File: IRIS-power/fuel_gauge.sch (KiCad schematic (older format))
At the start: 10 parts

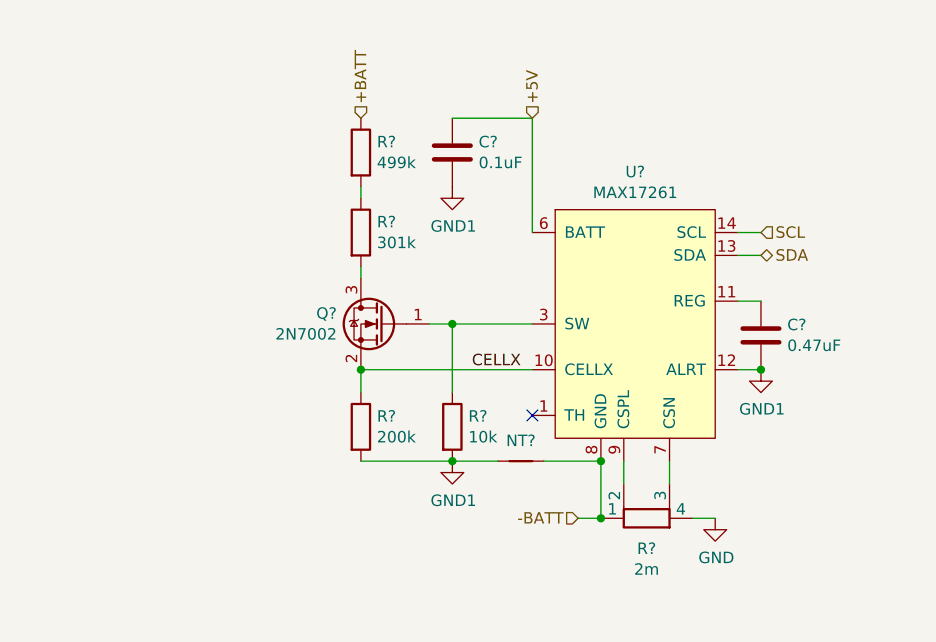
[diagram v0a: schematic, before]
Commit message: Finalized power board V2 schematic, preparing to layout
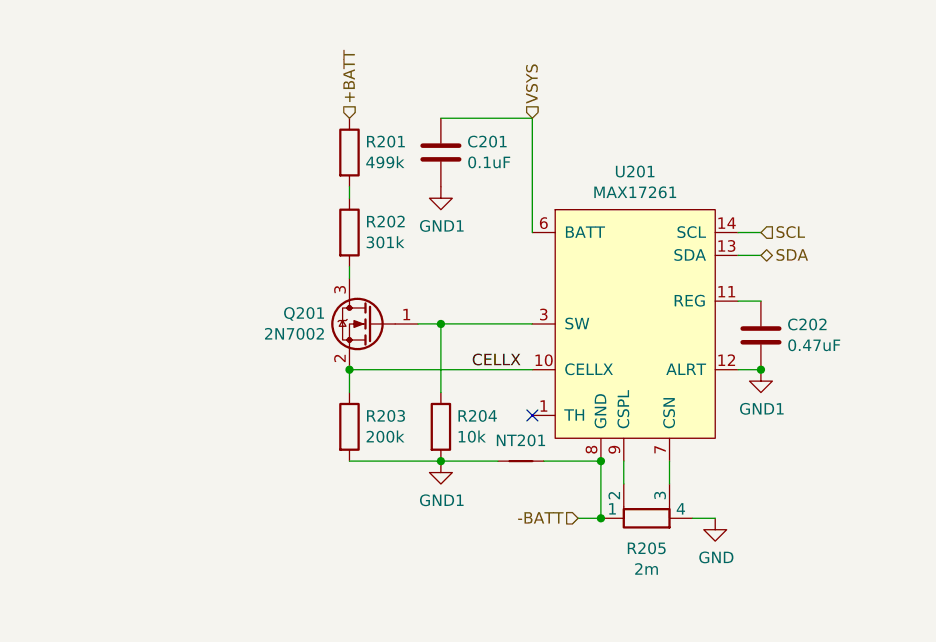
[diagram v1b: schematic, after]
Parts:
- C201, C202: renamed from C?; footprint (none) -> Capacitor_SMD:C_0603_1608Metric
- NT201: renamed from NT?; footprint (none) -> NetTie:NetTie-2_SMD_Pad0.5mm
- R201, R202, R203, R204: renamed from R?; footprint (none) -> Resistor_SMD:R_0603_1608Metric
- R205: renamed from R?; footprint (none) -> star-common-lib:CST0612-FC-R002E; Digikey PN (none) -> CST0612-FC-R002ECT-ND; MFG PN (none) -> CST0612-FC-R002E; Unit Cost (none) -> 0.78
- U201: renamed from U?; footprint (none) -> Package_DFN_QFN:DFN-14-1EP_3x3mm_P0.4mm_EP1.78x2.35mm
- gave numbers to parts that had none: 1
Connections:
- net +5V renamed VSYS
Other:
- moved on the sheet: C201, Q201, R201, R202, R203, R204
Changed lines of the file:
@@
 $Descr A4 11693 8268
 encoding utf-8
-Sheet 7 9
+Sheet 2 8
 Title ""
 Date ""
@@
 Wire Wire Line
 	5800 3100 5800 3600
-Wire Wire Line
-	5450 3100 5800 3100
 Text Label 5750 4200 2    50   ~ 0
 CELLX
 Wire Wire Line
-	5050 3450 5050 3400
-Wire Wire Line
-	5050 3750 5050 3800
+	5000 3450 5000 3400
+Wire Wire Line
+	5000 3750 5000 3800
 $Comp
 L power:GND1 #PWR?
 U 1 1 5F3ED548
-P 5450 4600
+P 5400 4600
 AR Path="/5F3ED548" Ref="#PWR?"  Part="1"
-AR Path="/5F3CDA08/5F3ED548" Ref="#PWR?"  Part="1"
-F 0 "#PWR?" H 5450 4350 50  0001 C CNN
-F 1 "GND1" H 5455 4427 50  0000 C CNN
-F 2 "" H 5450 4600 50  0001 C CNN
-F 3 "" H 5450 4600 50  0001 C CNN
-	1    5450 4600
+AR Path="/5F3CDA08/5F3ED548" Ref="#PWR0202"  Part="1"
+F 0 "#PWR0202" H 5400 4350 50  0001 C CNN
+F 1 "GND1" H 5405 4427 50  0000 C CNN
+F 2 "" H 5400 4600 50  0001 C CNN
+F 3 "" H 5400 4600 50  0001 C CNN
+	1    5400 4600
 	1    0    0    -1
 $EndComp
@@
 P 6800 4200
 AR Path="/5F3ED54F" Ref="#PWR?"  Part="1"
-AR Path="/5F3CDA08/5F3ED54F" Ref="#PWR?"  Part="1"
-F 0 "#PWR?" H 6800 3950 50  0001 C CNN
+AR Path="/5F3CDA08/5F3ED54F" Ref="#PWR0204"  Part="1"
+F 0 "#PWR0204" H 6800 3950 50  0001 C CNN
 F 1 "GND1" H 6805 4027 50  0000 C CNN
 F 2 "" H 6800 4200 50  0001 C CNN
@@
 L power:GND1 #PWR?
 U 1 1 5F3ED555
-P 5450 3400
+P 5400 3400
 AR Path="/5F3ED555" Ref="#PWR?"  Part="1"
-AR Path="/5F3CDA08/5F3ED555" Ref="#PWR?"  Part="1"
-F 0 "#PWR?" H 5450 3150 50  0001 C CNN
-F 1 "GND1" H 5455 3227 50  0000 C CNN
-F 2 "" H 5450 3400 50  0001 C CNN
-F 3 "" H 5450 3400 50  0001 C CNN
-	1    5450 3400
+AR Path="/5F3CDA08/5F3ED555" Ref="#PWR0201"  Part="1"
+F 0 "#PWR0201" H 5400 3150 50  0001 C CNN
+F 1 "GND1" H 5405 3227 50  0000 C CNN
+F 2 "" H 5400 3400 50  0001 C CNN
+F 3 "" H 5400 3400 50  0001 C CNN
+	1    5400 3400
 	1    0    0    -1
 $EndComp
@@
 P 5750 4600
 AR Path="/5F3ED55B" Ref="NT?"  Part="1"
-AR Path="/5F3CDA08/5F3ED55B" Ref="NT?"  Part="1"
-F 0 "NT?" H 5750 4689 50  0000 C CNN
+AR Path="/5F3CDA08/5F3ED55B" Ref="NT201"  Part="1"
+F 0 "NT201" H 5750 4689 50  0000 C CNN
 F 1 "Net-Tie_2" H 5750 4690 50  0001 C CNN
-F 2 "" H 5750 4600 50  0001 C CNN
+F 2 "NetTie:NetTie-2_SMD_Pad0.5mm" H 5750 4600 50  0001 C CNN
 F 3 "~" H 5750 4600 50  0001 C CNN
 	1    5750 4600
@@
 P 6600 4850
 AR Path="/5F3ED567" Ref="#PWR?"  Part="1"
-AR Path="/5F3CDA08/5F3ED567" Ref="#PWR?"  Part="1"
-F 0 "#PWR?" H 6600 4600 50  0001 C CNN
+AR Path="/5F3CDA08/5F3ED567" Ref="#PWR0203"  Part="1"
+F 0 "#PWR0203" H 6600 4600 50  0001 C CNN
 F 1 "GND" H 6605 4677 50  0000 C CNN
 F 2 "" H 6600 4850 50  0001 C CNN
@@
 L Device:R R?
 U 1 1 5F3ED56F
-P 5450 4450
+P 5400 4450
 AR Path="/5F3ED56F" Ref="R?"  Part="1"
-AR Path="/5F3CDA08/5F3ED56F" Ref="R?"  Part="1"
-F 0 "R?" H 5520 4496 50  0000 L CNN
-F 1 "10k" H 5520 4405 50  0000 L CNN
-F 2 "" V 5380 4450 50  0001 C CNN
-F 3 "~" H 5450 4450 50  0001 C CNN
-	1    5450 4450
+AR Path="/5F3CDA08/5F3ED56F" Ref="R204"  Part="1"
+F 0 "R204" H 5470 4496 50  0000 L CNN
+F 1 "10k" H 5470 4405 50  0000 L CNN
+F 2 "Resistor_SMD:R_0603_1608Metric" V 5330 4450 50  0001 C CNN
+F 3 "~" H 5400 4450 50  0001 C CNN
+	1    5400 4450
 	1    0    0    -1
 $EndComp
@@
 L Device:C C?
 U 1 1 5F3ED575
-P 5450 3250
+P 5400 3250
 AR Path="/5F3ED575" Ref="C?"  Part="1"
-AR Path="/5F3CDA08/5F3ED575" Ref="C?"  Part="1"
-F 0 "C?" H 5565 3296 50  0000 L CNN
-F 1 "0.1uF" H 5565 3205 50  0000 L CNN
-F 2 "" H 5488 3100 50  0001 C CNN
-F 3 "~" H 5450 3250 50  0001 C CNN
-	1    5450 3250
+AR Path="/5F3CDA08/5F3ED575" Ref="C201"  Part="1"
+F 0 "C201" H 5515 3296 50  0000 L CNN
+F 1 "0.1uF" H 5515 3205 50  0000 L CNN
+F 2 "Capacitor_SMD:C_0603_1608Metric" H 5438 3100 50  0001 C CNN
+F 3 "~" H 5400 3250 50  0001 C CNN
+	1    5400 3250
 	1    0    0    -1
 $EndComp
@@
 P 6800 4050
 AR Path="/5F3ED581" Ref="C?"  Part="1"
-AR Path="/5F3CDA08/5F3ED581" Ref="C?"  Part="1"
-F 0 "C?" H 6915 4096 50  0000 L CNN
+AR Path="/5F3CDA08/5F3ED581" Ref="C202"  Part="1"
+F 0 "C202" H 6915 4096 50  0000 L CNN
 F 1 "0.47uF" H 6915 4005 50  0000 L CNN
-F 2 "" H 6838 3900 50  0001 C CNN
+F 2 "Capacitor_SMD:C_0603_1608Metric" H 6838 3900 50  0001 C CNN
 F 3 "~" H 6800 4050 50  0001 C CNN
 	1    6800 4050
@@
 $EndComp
 Wire Wire Line
-	5050 4300 5050 4200
+	5000 4300 5000 4200
 $Comp
 L Device:R R?
 U 1 1 5F3ED58E
-P 5050 3250
+P 5000 3250
 AR Path="/5F3ED58E" Ref="R?"  Part="1"
-AR Path="/5F3CDA08/5F3ED58E" Ref="R?"  Part="1"
-F 0 "R?" H 5120 3296 50  0000 L CNN
-F 1 "499k" H 5120 3205 50  0000 L CNN
-F 2 "" V 4980 3250 50  0001 C CNN
-F 3 "~" H 5050 3250 50  0001 C CNN
-	1    5050 3250
+AR Path="/5F3CDA08/5F3ED58E" Ref="R201"  Part="1"
+F 0 "R201" H 5070 3296 50  0000 L CNN
+F 1 "499k" H 5070 3205 50  0000 L CNN
+F 2 "Resistor_SMD:R_0603_1608Metric" V 4930 3250 50  0001 C CNN
+F 3 "~" H 5000 3250 50  0001 C CNN
+	1    5000 3250
 	1    0    0    -1
 $EndComp
@@
 L Device:R R?
 U 1 1 5F3ED594
-P 5050 3600
+P 5000 3600
 AR Path="/5F3ED594" Ref="R?"  Part="1"
-AR Path="/5F3CDA08/5F3ED594" Ref="R?"  Part="1"
-F 0 "R?" H 5120 3646 50  0000 L CNN
-F 1 "301k" H 5120 3555 50  0000 L CNN
-F 2 "" V 4980 3600 50  0001 C CNN
-F 3 "~" H 5050 3600 50  0001 C CNN
-	1    5050 3600
+AR Path="/5F3CDA08/5F3ED594" Ref="R202"  Part="1"
+F 0 "R202" H 5070 3646 50  0000 L CNN
+F 1 "301k" H 5070 3555 50  0000 L CNN
+F 2 "Resistor_SMD:R_0603_1608Metric" V 4930 3600 50  0001 C CNN
+F 3 "~" H 5000 3600 50  0001 C CNN
+	1    5000 3600
 	1    0    0    -1
 $EndComp
@@
 L Device:R R?
 U 1 1 5F3ED59A
-P 5050 4450
+P 5000 4450
 AR Path="/5F3ED59A" Ref="R?"  Part="1"
-AR Path="/5F3CDA08/5F3ED59A" Ref="R?"  Part="1"
-F 0 "R?" H 5120 4496 50  0000 L CNN
-F 1 "200k" H 5120 4405 50  0000 L CNN
-F 2 "" V 4980 4450 50  0001 C CNN
-F 3 "~" H 5050 4450 50  0001 C CNN
-	1    5050 4450
+AR Path="/5F3CDA08/5F3ED59A" Ref="R203"  Part="1"
+F 0 "R203" H 5070 4496 50  0000 L CNN
+F 1 "200k" H 5070 4405 50  0000 L CNN
+F 2 "Resistor_SMD:R_0603_1608Metric" V 4930 4450 50  0001 C CNN
+F 3 "~" H 5000 4450 50  0001 C CNN
+	1    5000 4450
 	1    0    0    -1
 $EndComp
@@
 L Transistor_FET:2N7002 Q?
 U 1 1 5F3ED5A0
-P 5150 4000
+P 5100 4000
 AR Path="/5F3ED5A0" Ref="Q?"  Part="1"
-AR Path="/5F3CDA08/5F3ED5A0" Ref="Q?"  Part="1"
-F 0 "Q?" H 5355 4046 50  0000 L CNN
-F 1 "2N7002" H 5355 3955 50  0000 L CNN
-F 2 "Package_TO_SOT_SMD:SOT-23" H 5350 3925 50  0001 L CIN
-F 3 "https://www.fairchildsemi.com/datasheets/2N/2N7002.pdf" H 5150 4000 50  0001 L CNN
-	1    5150 4000
+AR Path="/5F3CDA08/5F3ED5A0" Ref="Q201"  Part="1"
+F 0 "Q201" H 5305 4046 50  0000 L CNN
+F 1 "2N7002" H 5305 3955 50  0000 L CNN
+F 2 "Package_TO_SOT_SMD:SOT-23" H 5300 3925 50  0001 L CIN
+F 3 "https://www.fairchildsemi.com/datasheets/2N/2N7002.pdf" H 5100 4000 50  0001 L CNN
+	1    5100 4000
 	-1   0    0    -1
 $EndComp
@@
 P 6300 4850
 AR Path="/5F3ED5AE" Ref="R?"  Part="1"
-AR Path="/5F3CDA08/5F3ED5AE" Ref="R?"  Part="1"
-F 0 "R?" V 6167 4850 50  0000 C CNN
+AR Path="/5F3CDA08/5F3ED5AE" Ref="R205"  Part="1"
+F 0 "R205" V 6167 4850 50  0000 C CNN
 F 1 "2m" V 6076 4850 50  0000 C CNN
-F 2 "" V 6230 4850 50  0001 C CNN
-F 3 "~" H 6300 4850 50  0001 C CNN
+F 2 "star-common-lib:CST0612-FC-R002E" V 6230 4850 50  0001 C CNN
+F 3 "https://www.bourns.com/docs/product-datasheets/cst0612.pdf" H 6300 4850 50  0001 C CNN
+F 4 "CST0612-FC-R002ECT-ND" H 6300 4850 50  0001 C CNN "Digikey PN"
+F 5 "CST0612-FC-R002E" H 6300 4850 50  0001 C CNN "MFG PN"
+F 6 "0.78" H 6300 4850 50  0001 C CNN "Unit Cost"
 	1    6300 4850
 	0    -1   -1   0
@@
 P 6250 4000
 AR Path="/5F3ED5B4" Ref="U?"  Part="1"
-AR Path="/5F3CDA08/5F3ED5B4" Ref="U?"  Part="1"
-F 0 "U?" H 6250 4665 50  0000 C CNN
+AR Path="/5F3CDA08/5F3ED5B4" Ref="U201"  Part="1"
+F 0 "U201" H 6250 4665 50  0000 C CNN
 F 1 "MAX17261" H 6250 4574 50  0000 C CNN
-F 2 "" H 6250 4000 50  0001 C CNN
+F 2 "Package_DFN_QFN:DFN-14-1EP_3x3mm_P0.4mm_EP1.78x2.35mm" H 6250 4000 50  0001 C CNN
 F 3 "" H 6250 4000 50  0001 C CNN
 	1    6250 4000
@@
 $EndComp
 Wire Wire Line
-	5450 4300 5450 4000
-Wire Wire Line
-	5800 4200 5050 4200
-Connection ~ 5050 4200
-Connection ~ 5450 4000
-Wire Wire Line
-	5450 4000 5800 4000
-Connection ~ 5450 4600
-Wire Wire Line
-	5450 4600 5650 4600
-Wire Wire Line
-	5350 4000 5450 4000
-Wire Wire Line
-	5050 4600 5450 4600
-Text HLabel 5050 3100 1    50   Input ~ 0
+	5400 4300 5400 4000
+Connection ~ 5000 4200
+Connection ~ 5400 4000
+Connection ~ 5400 4600
+Wire Wire Line
+	5300 4000 5400 4000
+Wire Wire Line
+	5000 4600 5400 4600
+Text HLabel 5000 3100 1    50   Input ~ 0
 +BATT
-Text HLabel 5800 3100 1    50   Input ~ 0
-+5V
 Text HLabel 6000 4850 0    50   Input ~ 0
 -BATT
@@
 Wire Wire Line
 	6700 3700 6800 3700
+Text HLabel 5800 3100 1    50   Input ~ 0
+VSYS
+Wire Wire Line
+	5400 4600 5650 4600
+Wire Wire Line
+	5000 4200 5800 4200
+Wire Wire Line
+	5400 4000 5800 4000
+Wire Wire Line
+	5400 3100 5800 3100
 $EndSCHEMATC

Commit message: Updated layout
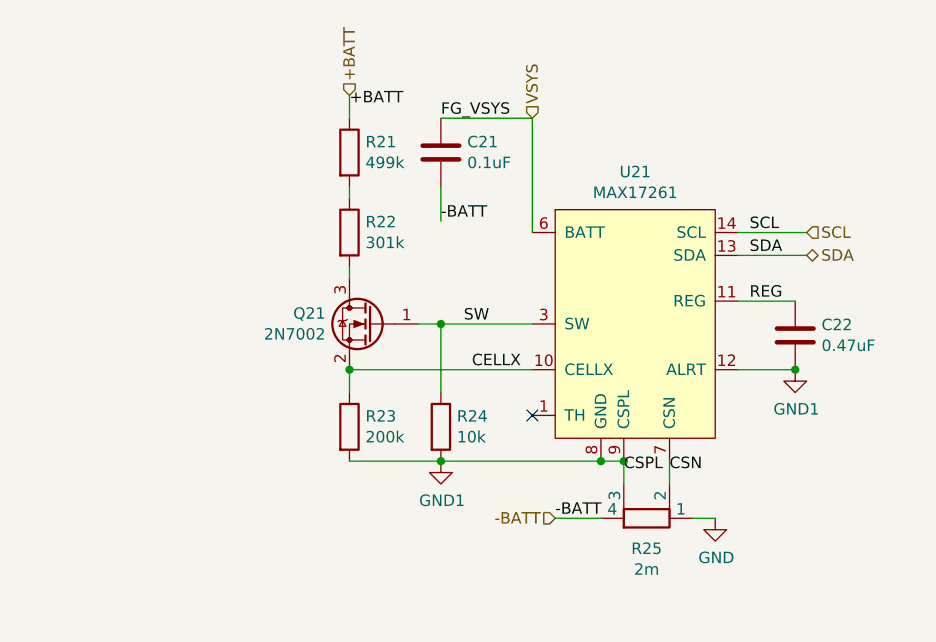
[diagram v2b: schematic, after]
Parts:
- removed NT201: Net-Tie_2, NetTie:NetTie-2_SMD_Pad0.5mm, symbol Device:Net-Tie_2
- U21: renamed from U201; footprint Package_DFN_QFN:DFN-14-1EP_3x3mm_P0.4mm_EP1.78x2.35mm -> star-common-lib:MAX17261
- renumbered C201 to C21, C202 to C22, Q201 to Q21, R201 to R21, R202 to R22, R203 to R23, R204 to R24, R205 to R25
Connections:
- net -BATT: now also C21.2, R25.4; no longer R25.1, U21.15, U21.8 (GND)
- net GND: now also R25.1; no longer R25.4
- net GND1: now also R25.3, U21.15, U21.8 (GND), U21.9 (CSPL); no longer C21.2
- net SW: now reaches Q21.1 (G), R24.1, U21.3 (SW)
- net REG: now reaches C22.1, U21.11 (REG)
- net CSN: now reaches R25.2
- net CSN: now also U21.7 (CSN); no longer U21.9 (CSPL)
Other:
- moved on the sheet: C22
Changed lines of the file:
@@
 P 5400 4600
 AR Path="/5F3ED548" Ref="#PWR?"  Part="1"
-AR Path="/5F3CDA08/5F3ED548" Ref="#PWR0202"  Part="1"
-F 0 "#PWR0202" H 5400 4350 50  0001 C CNN
+AR Path="/5F3CDA08/5F3ED548" Ref="#PWR021"  Part="1"
+F 0 "#PWR021" H 5400 4350 50  0001 C CNN
 F 1 "GND1" H 5405 4427 50  0000 C CNN
 F 2 "" H 5400 4600 50  0001 C CNN
@@
 	1    0    0    -1
 $EndComp
-Connection ~ 6800 4200
+Connection ~ 6950 4200
 $Comp
 L power:GND1 #PWR?
 U 1 1 5F3ED54F
-P 6800 4200
+P 6950 4200
 AR Path="/5F3ED54F" Ref="#PWR?"  Part="1"
-AR Path="/5F3CDA08/5F3ED54F" Ref="#PWR0204"  Part="1"
-F 0 "#PWR0204" H 6800 3950 50  0001 C CNN
-F 1 "GND1" H 6805 4027 50  0000 C CNN
-F 2 "" H 6800 4200 50  0001 C CNN
-F 3 "" H 6800 4200 50  0001 C CNN
-	1    6800 4200
-	1    0    0    -1
-$EndComp
-$Comp
-L power:GND1 #PWR?
-U 1 1 5F3ED555
-P 5400 3400
-AR Path="/5F3ED555" Ref="#PWR?"  Part="1"
-AR Path="/5F3CDA08/5F3ED555" Ref="#PWR0201"  Part="1"
-F 0 "#PWR0201" H 5400 3150 50  0001 C CNN
-F 1 "GND1" H 5405 3227 50  0000 C CNN
-F 2 "" H 5400 3400 50  0001 C CNN
-F 3 "" H 5400 3400 50  0001 C CNN
-	1    5400 3400
-	1    0    0    -1
-$EndComp
-$Comp
-L Device:Net-Tie_2 NT?
-U 1 1 5F3ED55B
-P 5750 4600
-AR Path="/5F3ED55B" Ref="NT?"  Part="1"
-AR Path="/5F3CDA08/5F3ED55B" Ref="NT201"  Part="1"
-F 0 "NT201" H 5750 4689 50  0000 C CNN
-F 1 "Net-Tie_2" H 5750 4690 50  0001 C CNN
-F 2 "NetTie:NetTie-2_SMD_Pad0.5mm" H 5750 4600 50  0001 C CNN
-F 3 "~" H 5750 4600 50  0001 C CNN
-	1    5750 4600
+AR Path="/5F3CDA08/5F3ED54F" Ref="#PWR023"  Part="1"
+F 0 "#PWR023" H 6950 3950 50  0001 C CNN
+F 1 "GND1" H 6955 4027 50  0000 C CNN
+F 2 "" H 6950 4200 50  0001 C CNN
+F 3 "" H 6950 4200 50  0001 C CNN
+	1    6950 4200
 	1    0    0    -1
 $EndComp
@@
 P 6600 4850
 AR Path="/5F3ED567" Ref="#PWR?"  Part="1"
-AR Path="/5F3CDA08/5F3ED567" Ref="#PWR0203"  Part="1"
-F 0 "#PWR0203" H 6600 4600 50  0001 C CNN
+AR Path="/5F3CDA08/5F3ED567" Ref="#PWR022"  Part="1"
+F 0 "#PWR022" H 6600 4600 50  0001 C CNN
 F 1 "GND" H 6605 4677 50  0000 C CNN
 F 2 "" H 6600 4850 50  0001 C CNN
@@
 	1    0    0    -1
 $EndComp
-Wire Wire Line
-	6700 4200 6800 4200
 NoConn ~ 5800 4400
 $Comp
@@
 P 5400 4450
 AR Path="/5F3ED56F" Ref="R?"  Part="1"
-AR Path="/5F3CDA08/5F3ED56F" Ref="R204"  Part="1"
-F 0 "R204" H 5470 4496 50  0000 L CNN
+AR Path="/5F3CDA08/5F3ED56F" Ref="R24"  Part="1"
+F 0 "R24" H 5470 4496 50  0000 L CNN
 F 1 "10k" H 5470 4405 50  0000 L CNN
 F 2 "Resistor_SMD:R_0603_1608Metric" V 5330 4450 50  0001 C CNN
@@
 P 5400 3250
 AR Path="/5F3ED575" Ref="C?"  Part="1"
-AR Path="/5F3CDA08/5F3ED575" Ref="C201"  Part="1"
-F 0 "C201" H 5515 3296 50  0000 L CNN
+AR Path="/5F3CDA08/5F3ED575" Ref="C21"  Part="1"
+F 0 "C21" H 5515 3296 50  0000 L CNN
 F 1 "0.1uF" H 5515 3205 50  0000 L CNN
 F 2 "Capacitor_SMD:C_0603_1608Metric" H 5438 3100 50  0001 C CNN
@@
 	1    0    0    -1
 $EndComp
-Wire Wire Line
-	6700 3900 6800 3900
 $Comp
 L Device:C C?
 U 1 1 5F3ED581
-P 6800 4050
+P 6950 4050
 AR Path="/5F3ED581" Ref="C?"  Part="1"
-AR Path="/5F3CDA08/5F3ED581" Ref="C202"  Part="1"
-F 0 "C202" H 6915 4096 50  0000 L CNN
-F 1 "0.47uF" H 6915 4005 50  0000 L CNN
-F 2 "Capacitor_SMD:C_0603_1608Metric" H 6838 3900 50  0001 C CNN
-F 3 "~" H 6800 4050 50  0001 C CNN
-	1    6800 4050
+AR Path="/5F3CDA08/5F3ED581" Ref="C22"  Part="1"
+F 0 "C22" H 7065 4096 50  0000 L CNN
+F 1 "0.47uF" H 7065 4005 50  0000 L CNN
+F 2 "Capacitor_SMD:C_0603_1608Metric" H 6988 3900 50  0001 C CNN
+F 3 "~" H 6950 4050 50  0001 C CNN
+	1    6950 4050
 	1    0    0    -1
 $EndComp
@@
 P 5000 3250
 AR Path="/5F3ED58E" Ref="R?"  Part="1"
-AR Path="/5F3CDA08/5F3ED58E" Ref="R201"  Part="1"
-F 0 "R201" H 5070 3296 50  0000 L CNN
+AR Path="/5F3CDA08/5F3ED58E" Ref="R21"  Part="1"
+F 0 "R21" H 5070 3296 50  0000 L CNN
 F 1 "499k" H 5070 3205 50  0000 L CNN
 F 2 "Resistor_SMD:R_0603_1608Metric" V 4930 3250 50  0001 C CNN
@@
 P 5000 3600
 AR Path="/5F3ED594" Ref="R?"  Part="1"
-AR Path="/5F3CDA08/5F3ED594" Ref="R202"  Part="1"
-F 0 "R202" H 5070 3646 50  0000 L CNN
+AR Path="/5F3CDA08/5F3ED594" Ref="R22"  Part="1"
+F 0 "R22" H 5070 3646 50  0000 L CNN
 F 1 "301k" H 5070 3555 50  0000 L CNN
 F 2 "Resistor_SMD:R_0603_1608Metric" V 4930 3600 50  0001 C CNN
@@
 P 5000 4450
 AR Path="/5F3ED59A" Ref="R?"  Part="1"
-AR Path="/5F3CDA08/5F3ED59A" Ref="R203"  Part="1"
-F 0 "R203" H 5070 4496 50  0000 L CNN
+AR Path="/5F3CDA08/5F3ED59A" Ref="R23"  Part="1"
+F 0 "R23" H 5070 4496 50  0000 L CNN
 F 1 "200k" H 5070 4405 50  0000 L CNN
 F 2 "Resistor_SMD:R_0603_1608Metric" V 4930 4450 50  0001 C CNN
@@
 P 5100 4000
 AR Path="/5F3ED5A0" Ref="Q?"  Part="1"
-AR Path="/5F3CDA08/5F3ED5A0" Ref="Q201"  Part="1"
-F 0 "Q201" H 5305 4046 50  0000 L CNN
+AR Path="/5F3CDA08/5F3ED5A0" Ref="Q21"  Part="1"
+F 0 "Q21" H 5305 4046 50  0000 L CNN
 F 1 "2N7002" H 5305 3955 50  0000 L CNN
 F 2 "Package_TO_SOT_SMD:SOT-23" H 5300 3925 50  0001 L CIN
@@
 P 6300 4850
 AR Path="/5F3ED5AE" Ref="R?"  Part="1"
-AR Path="/5F3CDA08/5F3ED5AE" Ref="R205"  Part="1"
-F 0 "R205" V 6167 4850 50  0000 C CNN
+AR Path="/5F3CDA08/5F3ED5AE" Ref="R25"  Part="1"
+F 0 "R25" V 6167 4850 50  0000 C CNN
 F 1 "2m" V 6076 4850 50  0000 C CNN
 F 2 "star-common-lib:CST0612-FC-R002E" V 6230 4850 50  0001 C CNN
@@
 F 6 "0.78" H 6300 4850 50  0001 C CNN "Unit Cost"
 	1    6300 4850
-	0    -1   -1   0
-$EndComp
+	0    1    -1   0
+$EndComp
+Wire Wire Line
+	5400 4300 5400 4000
+Connection ~ 5000 4200
+Connection ~ 5400 4000
+Connection ~ 5400 4600
+Wire Wire Line
+	5300 4000 5400 4000
+Wire Wire Line
+	5000 4600 5400 4600
+Text HLabel 5000 3000 1    50   Input ~ 0
++BATT
+Text HLabel 5900 4850 0    50   Input ~ 0
+-BATT
+Wire Wire Line
+	6600 4850 6500 4850
+Text HLabel 7000 3600 2    50   Input ~ 0
+SCL
+Text HLabel 7000 3700 2    50   BiDi ~ 0
+SDA
+Text HLabel 5800 3100 1    50   Input ~ 0
+VSYS
+Wire Wire Line
+	5000 4200 5800 4200
+Wire Wire Line
+	5400 4000 5800 4000
+Wire Wire Line
+	5400 3100 5800 3100
+Text Label 5500 4000 0    50   ~ 0
+SW
+Text Label 6750 3900 0    50   ~ 0
+REG
+Wire Wire Line
+	6700 3900 6950 3900
+Wire Wire Line
+	6700 4200 6950 4200
+Text Label 6200 4650 0    50   ~ 0
+CSPL
+Text Label 6400 4650 0    50   ~ 0
+CSN
+Wire Wire Line
+	5000 3000 5000 3100
+Text Label 5000 3050 0    50   ~ 0
++BATT
+Connection ~ 6200 4600
+Wire Wire Line
+	6100 4600 6200 4600
+Connection ~ 6100 4600
 $Comp
 L star-common-lib:MAX17261 U?
@@
 P 6250 4000
 AR Path="/5F3ED5B4" Ref="U?"  Part="1"
-AR Path="/5F3CDA08/5F3ED5B4" Ref="U201"  Part="1"
-F 0 "U201" H 6250 4665 50  0000 C CNN
+AR Path="/5F3CDA08/5F3ED5B4" Ref="U21"  Part="1"
+F 0 "U21" H 6250 4665 50  0000 C CNN
 F 1 "MAX17261" H 6250 4574 50  0000 C CNN
-F 2 "Package_DFN_QFN:DFN-14-1EP_3x3mm_P0.4mm_EP1.78x2.35mm" H 6250 4000 50  0001 C CNN
+F 2 "star-common-lib:MAX17261" H 6250 4000 50  0001 C CNN
 F 3 "" H 6250 4000 50  0001 C CNN
 	1    6250 4000
@@
 $EndComp
 Wire Wire Line
-	5400 4300 5400 4000
-Connection ~ 5000 4200
-Connection ~ 5400 4000
-Connection ~ 5400 4600
-Wire Wire Line
-	5300 4000 5400 4000
-Wire Wire Line
-	5000 4600 5400 4600
-Text HLabel 5000 3100 1    50   Input ~ 0
-+BATT
-Text HLabel 6000 4850 0    50   Input ~ 0
+	5400 4600 6100 4600
+Wire Wire Line
+	5900 4850 6100 4850
+Text Label 5900 4850 0    50   ~ 0
 -BATT
-Wire Wire Line
-	6100 4850 6000 4850
-Wire Wire Line
-	6100 4850 6100 4600
-Connection ~ 6100 4850
-Wire Wire Line
-	6100 4600 5850 4600
-Connection ~ 6100 4600
-Wire Wire Line
-	6600 4850 6500 4850
-Text HLabel 6800 3600 2    50   Input ~ 0
+Text Label 5400 3550 0    50   ~ 0
+-BATT
+Wire Wire Line
+	5400 3550 5400 3400
+Wire Wire Line
+	6700 3600 7000 3600
+Wire Wire Line
+	6700 3700 7000 3700
+Text Label 6750 3600 0    50   ~ 0
 SCL
-Text HLabel 6800 3700 2    50   BiDi ~ 0
+Text Label 6750 3700 0    50   ~ 0
 SDA
-Wire Wire Line
-	6800 3600 6700 3600
-Wire Wire Line
-	6700 3700 6800 3700
-Text HLabel 5800 3100 1    50   Input ~ 0
-VSYS
-Wire Wire Line
-	5400 4600 5650 4600
-Wire Wire Line
-	5000 4200 5800 4200
-Wire Wire Line
-	5400 4000 5800 4000
-Wire Wire Line
-	5400 3100 5800 3100
+Text Label 5400 3100 0    50   ~ 0
+FG_VSYS
 $EndSCHEMATC
